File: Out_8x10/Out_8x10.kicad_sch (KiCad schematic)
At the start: 82 parts, among them J1 Conn_01x06, J2 nmount SW Debug, J3 USB_C_Receptacle_USB2.0, J4 Conn_01x06, SW1 Reset, SW2 Boot, SW3 ADDRESS, U1 ADM3483, U14 LMV321, U2 W25Q128JVSIQ, U3 RP2040, U4 SN74AHCT1G125, U5 AP2112K-3.3, Y1 12MHz,18pF

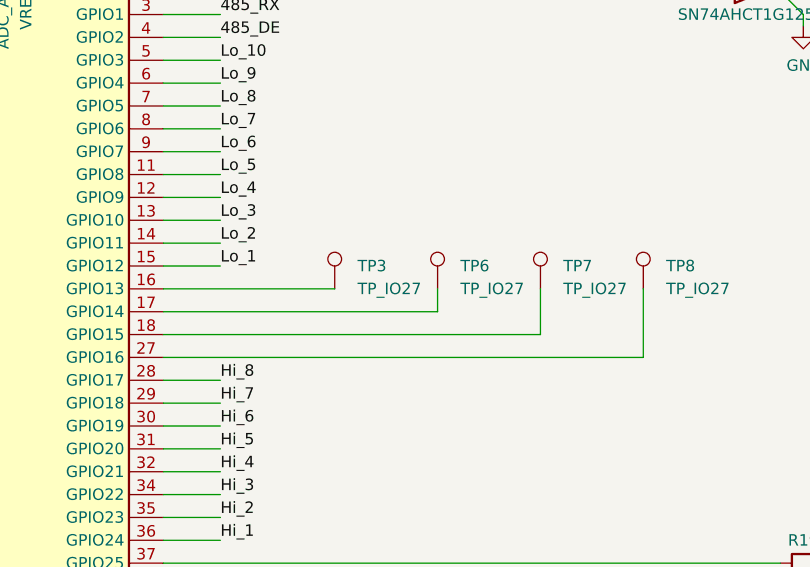
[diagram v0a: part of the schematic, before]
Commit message: TPs to RM2.54
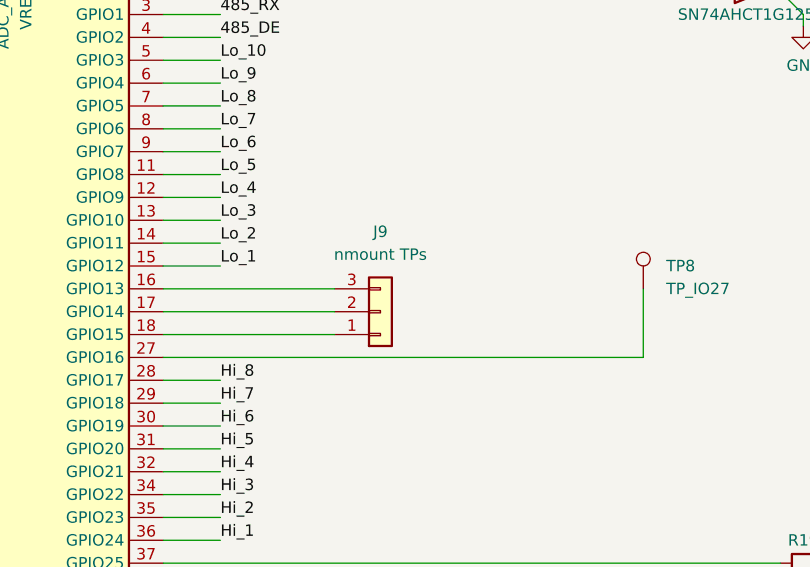
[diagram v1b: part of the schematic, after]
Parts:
- removed TP3, TP6, TP7: TP_IO27, TestPoint:TestPoint_Pad_D1.0mm, symbol Connector:TestPoint
- added J9: nmount TPs, Connector_PinSocket_2.54mm:PinSocket_1x03_P2.54mm_Vertical, symbol Connector_Generic:Conn_01x03
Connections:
- net at U3.17 (GPIO14): now also J9.2 (Pin_2)
- net at U3.16 (GPIO13): now also J9.3 (Pin_3)
- net at U3.18 (GPIO15): now also J9.1 (Pin_1)
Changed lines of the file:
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@@
     (title "Out_8x10")
     (date "2023-10-08")
-    (rev "00.20")
+    (rev "0.2.0")
   )
   (junction (at 247.65 219.71) (diameter 0) (color 0 0 0 0)
@@
     (stroke (width 0) (type default) (color 0 0 0 0))
   )
-  (wire (pts (xy 255.27 132.08) (xy 255.27 129.54))
-    (stroke (width 0) (type default) (color 0 0 0 0))
-  )
   (wire (pts (xy 278.13 137.16) (xy 278.13 129.54))
     (stroke (width 0) (type default) (color 0 0 0 0))
@@
     (stroke (width 0) (type default) (color 0 0 0 0))
   )
-  (wire (pts (xy 224.79 134.62) (xy 266.7 134.62))
-    (stroke (width 0) (type default) (color 0 0 0 0))
-  )
-  (wire (pts (xy 266.7 134.62) (xy 266.7 129.54))
+  (wire (pts (xy 224.79 134.62) (xy 243.84 134.62))
     (stroke (width 0) (type default) (color 0 0 0 0))
   )
@@
     (stroke (width 0) (type default) (color 0 0 0 0))
   )
-  (wire (pts (xy 224.79 132.08) (xy 255.27 132.08))
+  (wire (pts (xy 224.79 132.08) (xy 243.84 132.08))
     (stroke (width 0) (type default) (color 0 0 0 0))
   )
@@
     (pin "1")
   )
-  (symbol (lib_id "Connector:TestPoint") (at 255.27 129.54 0) (unit 1)
-    (in_bom yes) (on_board yes)
-    (property "Reference" "TP6" (id 0) (at 257.81 127 0)
-      (effects (font (size 1.27 1.27)) (justify left))
-    )
-    (property "Value" "TP_IO27" (id 1) (at 257.81 129.54 0)
-      (effects (font (size 1.27 1.27)) (justify left))
-    )
-    (property "Footprint" "TestPoint:TestPoint_Pad_D1.0mm" (id 2) (at 260.35 129.54 0)
-      (effects (font (size 1.27 1.27)) hide)
-    )
-    (property "Datasheet" "~" (id 3) (at 260.35 129.54 0)
-      (effects (font (size 1.27 1.27)) hide)
-    )
-    (pin "1")
-  )
   (symbol (lib_id "power:+5V") (at 323.85 73.66 0) (unit 1)
     (in_bom yes) (on_board yes)
@@
     (pin "2")
   )
-  (symbol (lib_id "Connector:TestPoint") (at 266.7 129.54 0) (unit 1)
-    (in_bom yes) (on_board yes)
-    (property "Reference" "TP7" (id 0) (at 269.24 127 0)
-      (effects (font (size 1.27 1.27)) (justify left))
-    )
-    (property "Value" "TP_IO27" (id 1) (at 269.24 129.54 0)
-      (effects (font (size 1.27 1.27)) (justify left))
-    )
-    (property "Footprint" "TestPoint:TestPoint_Pad_D1.0mm" (id 2) (at 271.78 129.54 0)
-      (effects (font (size 1.27 1.27)) hide)
-    )
-    (property "Datasheet" "~" (id 3) (at 271.78 129.54 0)
-      (effects (font (size 1.27 1.27)) hide)
-    )
-    (pin "1")
-  )
   (symbol (lib_id "Device:R") (at 68.58 73.66 0) (unit 1)
     (in_bom yes) (on_board yes)
@@
     (pin "2")
   )
-  (symbol (lib_id "Connector:TestPoint") (at 243.84 129.54 0) (unit 1)
-    (in_bom yes) (on_board yes)
-    (property "Reference" "TP3" (id 0) (at 246.38 127 0)
-      (effects (font (size 1.27 1.27)) (justify left))
-    )
-    (property "Value" "TP_IO27" (id 1) (at 246.38 129.54 0)
-      (effects (font (size 1.27 1.27)) (justify left))
-    )
-    (property "Footprint" "TestPoint:TestPoint_Pad_D1.0mm" (id 2) (at 248.92 129.54 0)
-      (effects (font (size 1.27 1.27)) hide)
-    )
-    (property "Datasheet" "~" (id 3) (at 248.92 129.54 0)
-      (effects (font (size 1.27 1.27)) hide)
-    )
-    (pin "1")
-  )
   (symbol (lib_id "power:+3V3") (at 339.09 27.94 0) (unit 1)
     (in_bom yes) (on_board yes)
@@
     (pin "6")
   )
+  (symbol (lib_id "Connector_Generic:Conn_01x03") (at 248.92 132.08 0) (mirror x) (unit 1)
+    (in_bom no) (on_board yes) (fields_autoplaced)
+    (property "Reference" "J9" (id 0) (at 248.92 123.19 0))
+    (property "Value" "nmount TPs" (id 1) (at 248.92 125.73 0))
+    (property "Footprint" "Connector_PinSocket_2.54mm:PinSocket_1x03_P2.54mm_Vertical" (id 2) (at 248.92 132.08 0)
+      (effects (font (size 1.27 1.27)) hide)
+    )
+    (property "Datasheet" "~" (id 3) (at 248.92 132.08 0)
+      (effects (font (size 1.27 1.27)) hide)
+    )
+    (pin "1")
+    (pin "2")
+    (pin "3")
+  )
   (symbol (lib_id "Device:R") (at 168.91 212.09 0) (unit 1)
     (in_bom yes) (on_board yes) (fields_autoplaced)
@@
       (reference "J8") (unit 1) (value "Conn_01x12") (footprint "Connector_Molex:Molex_KK-396_5273-12A_1x12_P3.96mm_Vertical")
     )
+    (path "/f068bde2-dac1-4292-8250-19a4d58715ed"
+      (reference "J9") (unit 1) (value "nmount TPs") (footprint "Connector_PinSocket_2.54mm:PinSocket_1x03_P2.54mm_Vertical")
+    )
     (path "/c9a975b0-1246-4730-bd1c-268dfbd64e4d/28b0a393-7d6d-4b6d-9404-1d0569a19195"
       (reference "Q1") (unit 1) (value "2N7002") (footprint "Package_TO_SOT_SMD:SOT-23")
@@
       (reference "TP2") (unit 1) (value "TP_IO27") (footprint "TestPoint:TestPoint_Pad_D1.0mm")
     )
-    (path "/be16ef5d-c832-41f8-90b1-f0d5d57341ca"
-      (reference "TP3") (unit 1) (value "TP_IO27") (footprint "TestPoint:TestPoint_Pad_D1.0mm")
-    )
     (path "/ddd8c900-4c7c-4ae4-ade4-c1575c4be8a8"
       (reference "TP4") (unit 1) (value "TP_LED") (footprint "Connector_Pin:Pin_D1.0mm_L10.0mm")
@@
       (reference "TP5") (unit 1) (value "TP_GND") (footprint "Connector_Pin:Pin_D1.0mm_L10.0mm")
     )
-    (path "/5261ae00-6c40-4e11-a298-8e7a88376e70"
-      (reference "TP6") (unit 1) (value "TP_IO27") (footprint "TestPoint:TestPoint_Pad_D1.0mm")
-    )
-    (path "/7d34d364-5189-4944-9a06-4e905225b496"
-      (reference "TP7") (unit 1) (value "TP_IO27") (footprint "TestPoint:TestPoint_Pad_D1.0mm")
-    )
     (path "/97d74989-a5d9-4cbf-aaa8-99fbaaefd34a"

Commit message: V1.0.0
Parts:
- removed F1: T500mA,<0.3Ω, Fuse:Fuse_1206_3216Metric, symbol Device:Fuse
- removed R3, R5: 1k, Resistor_SMD:R_0402_1005Metric, symbol Device:R
- added D7: 1A, Diode_SMD:D_SOD-323, symbol Device:D_Schottky
- added JP1: Jumper_2_Open, Connector_PinHeader_2.54mm:PinHeader_1x02_P2.54mm_Vertical, symbol Jumper:Jumper_2_Open
- C22: JLCPCB Rotation Offset (none) -> 180
- SW3, U5: JLCPCB Rotation Offset (none) -> 90
- TP4, TP5, TP8: now left out of the parts list
- U3: JLCPCB Rotation Offset (none) -> -90
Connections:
- net +5V: now also D7.1 (K)
- net 5V_IN: now also D7.2 (A)
- net A: now also J1.4 (Pin_4), JP1.2 (B); no longer R4.1
- net B: now also J1.5 (Pin_5)
- net GND: no longer J1.4 (Pin_4), J1.5 (Pin_5)
- new net: JP1.1 (A), R4.1
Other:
- moved on the sheet: D1
